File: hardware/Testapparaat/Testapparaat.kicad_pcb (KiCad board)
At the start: 2 copper layers, 127 x 142.2 mm, 115 parts, among them J1 IO_SD, J10 B-, J11 Display_shield, J12 GPIO_INPUTS, J13 FrontPanel, J14 GPIO_OUTPUT, J2 Module_1, J3 Module_2, J4 DEBUG, J5 FPC_40P_LCD_ILI9488, J6 IO_UART, J7 Emergency Stop Button, J8 CON-SOCJ-2155, J9 B+, Q1 BC817, Q2 BC817, Q3 BC817, Q4 IRFR9024N, Q5 IRFR9024N, Q6 IRFR9024N, SW1 RST, SW2 on/off switch, U1 74HC595 (SIPO Shift register), U10 LM2596S-5, U11 LM2596S-3.3, U12 74AUC1G74, U2 ESP32-WROOM-32, U4 74HC595 (SIPO Shift register), U5 TCA9534 (IO Expander), U6 74HC14, U7 TCA9534 (IO Expander), U8 74HC14, U9 74HC14

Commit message: -enh routed power section
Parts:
- C15, R19, R20: moved to B.Cu
- moved Q5 17.2 mm to (165.5, 38.3)
- moved R19 9.15 mm to (153.3, 98.2), turned to -90 degrees
- moved Q6 7.93 mm to (165.6, 45.2)
- moved Q4 6.73 mm to (165.7, 53.1)
- moved REF** 4.15 mm to (165.2, 29.5)
- moved C15 3.96 mm to (147.7, 93.3)
- moved R20 3.24 mm to (168.4, 51.7)
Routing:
- net +5VP: track 0.00 -> 39.7 mm
- net +VSW: track 0.00 -> 33.9 mm
- net +3.3VP: track 0.00 -> 20.1 mm

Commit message: -enh routed more power section
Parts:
- removed the REF** at (181.4, 124.4)
- C16, J14, R1, U4: moved to B.Cu
- moved R10 62.3 mm to (145.5, 157.2), turned to 180 degrees
- moved R9 59.0 mm to (148.0, 159.1), turned to 90 degrees
- moved C8 48.8 mm to (204.6, 133.9), turned to 90 degrees
- moved U11 38.5 mm to (163.8, 142.5), turned to 90 degrees
- moved J10 38.2 mm to (164.5, 124.4)
- moved L1 37.1 mm to (201.2, 143.3), turned to 90 degrees
- moved D1 36.1 mm to (199.9, 151.8), turned to 0 degrees
- moved C22 34.7 mm to (153.3, 36.5), turned to 90 degrees
- moved R7 31.9 mm to (151.5, 151.4)
- moved R8 30.8 mm to (150.1, 145.9)
- moved C9 27.5 mm to (179.9, 131.5), turned to 180 degrees
- moved C3 23.8 mm to (232.1, 131.7)
- moved R6 23.8 mm to (230.1, 133.0)
- moved D2 19.7 mm to (174.8, 151.5), turned to 0 degrees
- moved C2 18.3 mm to (192.6, 129.6)
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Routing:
- net +BATT: track 77.7 -> 211.1 mm
- net +5V: track 32.0 -> 160.2 mm, vias 1 -> 0
- net +VSW: track 33.9 -> 91.7 mm
- net +5VP: track 39.7 -> 96.8 mm
- net REG_EN: track 50.2 -> 0.00 mm, vias 2 -> 0
- net +3.3V: track 39.6 -> 81.7 mm, vias 1 -> 0
- net +3.3VP: track 20.1 -> 57.2 mm
- net Net-(Q3-Pad3): track 0.00 -> 22.7 mm, vias 0 -> 2
- net Net-(C2-Pad1): track 0.00 -> 22.3 mm
- net Net-(D1-Pad1): track 19.1 -> 0.00 mm
- net Net-(D4-Pad2): track 8.48 -> 0.00 mm
- net GND: track 7.77 -> 0.00 mm
- net Net-(R7-Pad2): track 7.62 -> 0.00 mm, vias 1 -> 0
- net Net-(R10-Pad1): track 6.44 -> 2.32 mm, vias 1 -> 0

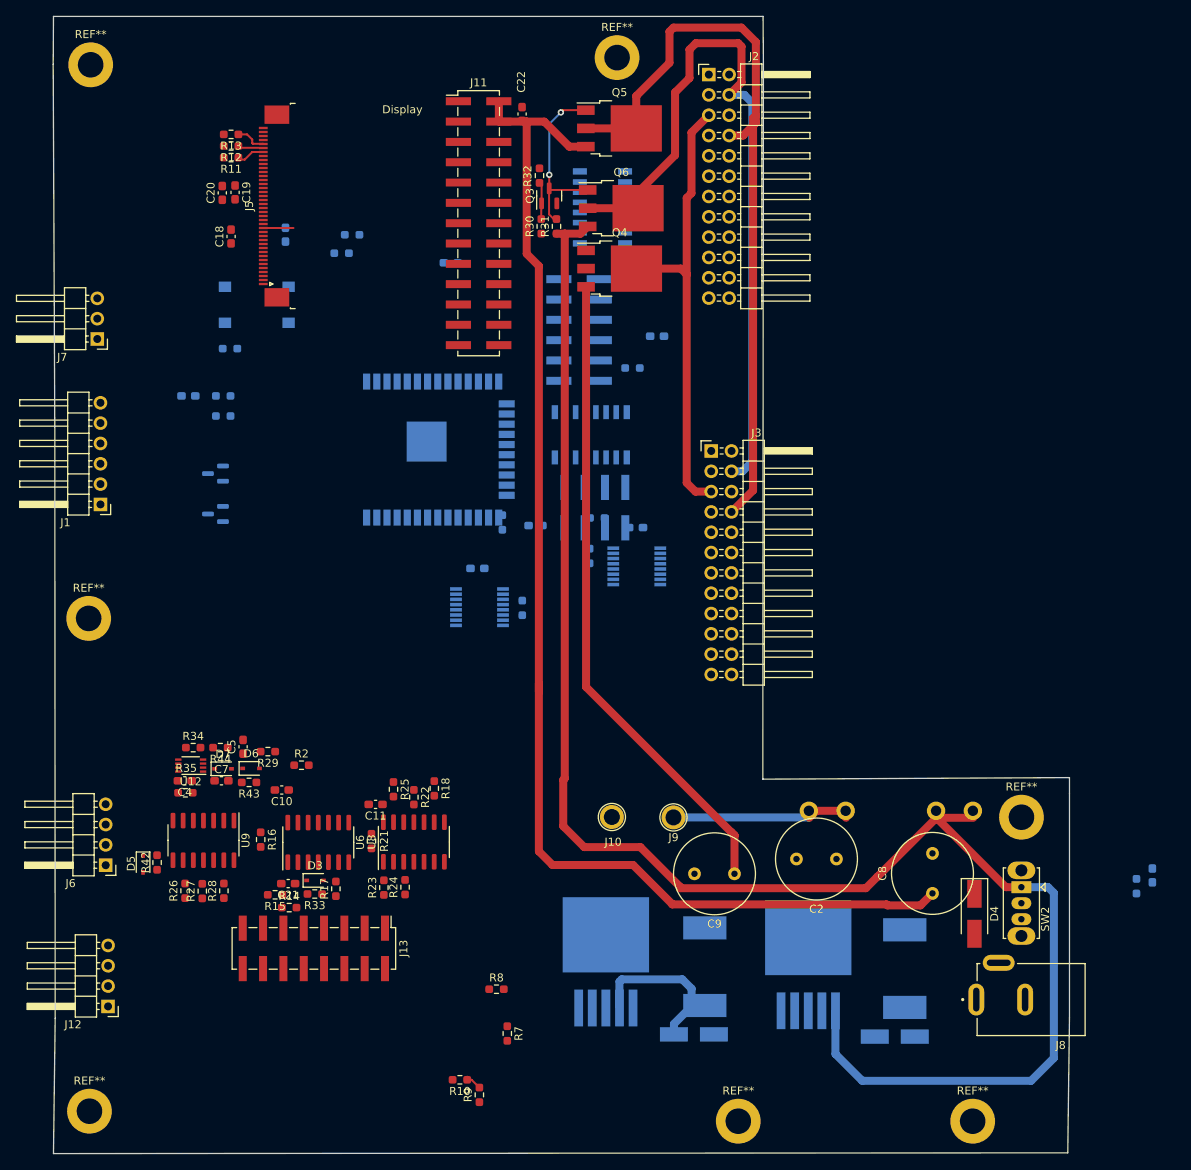
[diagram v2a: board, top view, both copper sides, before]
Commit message: -enh routed some of the module traces
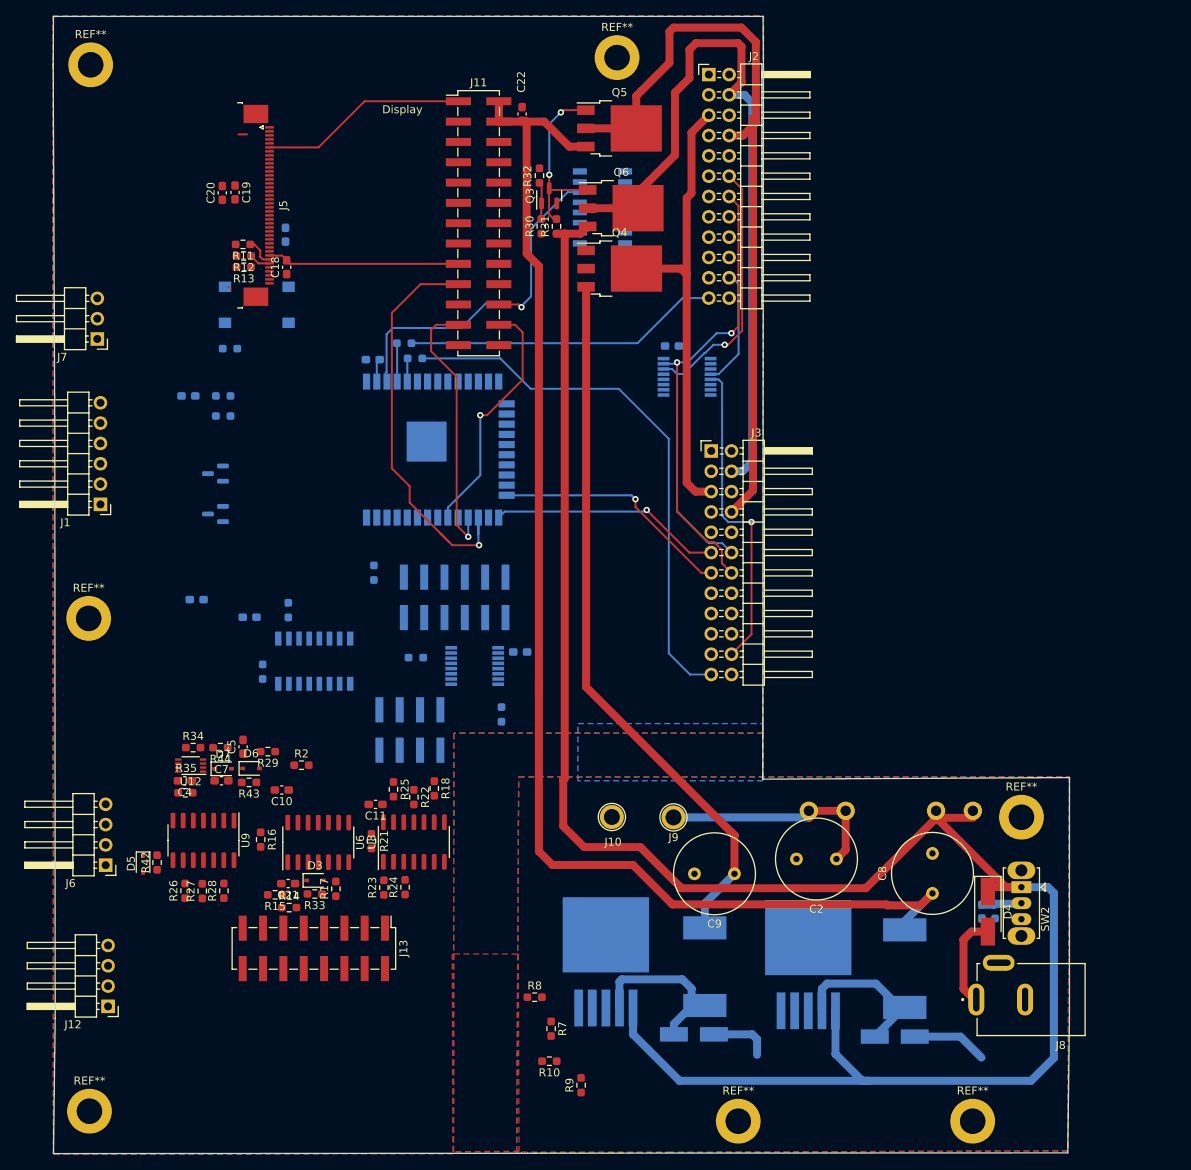
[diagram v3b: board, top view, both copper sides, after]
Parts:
- moved R1 52.6 mm to (124.1, 98.5), turned to -90 degrees
- moved U4 44.7 mm to (127.3, 104.9)
- moved U5 38.8 mm to (173.9, 69.4)
- moved C14 37.5 mm to (119.3, 99.4)
- moved J4 36.9 mm to (144.9, 96.9), turned to 90 degrees
- moved J14 36.2 mm to (139.3, 113.5)
- moved C15 35.3 mm to (112.6, 97.2)
- moved R19 33.4 mm to (120.9, 106.2)
- moved R40 28.6 mm to (140.0, 104.5)
- moved U7 23.8 mm to (147.4, 105.5)
- moved R41 22.7 mm to (150.7, 111.6)
- moved C3 21.8 mm to (210.8, 136.2)
- moved C17 21.3 mm to (153.1, 103.8)
- moved R6 17.9 mm to (212.4, 136.1)
- moved R36 17.3 mm to (139.9, 67.1)
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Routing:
- net ID_MOD_2: track 0.00 -> 68.2 mm
- net +3.3V: track 81.7 -> 142.9 mm
- net I2C_SCL: track 0.00 -> 58.4 mm, vias 0 -> 1
- net I2C_SDA: track 0.00 -> 57.6 mm, vias 0 -> 2
- net SPI_MOSI: track 0.00 -> 52.7 mm, vias 0 -> 1
- net TTL3_MOD_2: track 0.00 -> 39.8 mm, vias 0 -> 1
- net +BATT: track 211.1 -> 250.7 mm
- net ID_MOD_1: track 0.00 -> 39.5 mm
- net SPI_CLK: track 0.00 -> 33.9 mm, vias 0 -> 1
- net /Display/Display_CS: track 0.00 -> 30.9 mm, vias 0 -> 1
- net PWM2_MOD_2: track 0.00 -> 30.1 mm, vias 0 -> 1
- net PWM1_MOD_2: track 0.00 -> 29.2 mm, vias 0 -> 1
- net Net-(D1-Pad1): track 0.00 -> 19.9 mm
- net RESET: track 0.00 -> 19.1 mm
- net Display_RST: track 3.78 -> 21.3 mm, vias 0 -> 1
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- added copper zone on B.Cu, net GND
- added copper zone on F.Cu, net GND

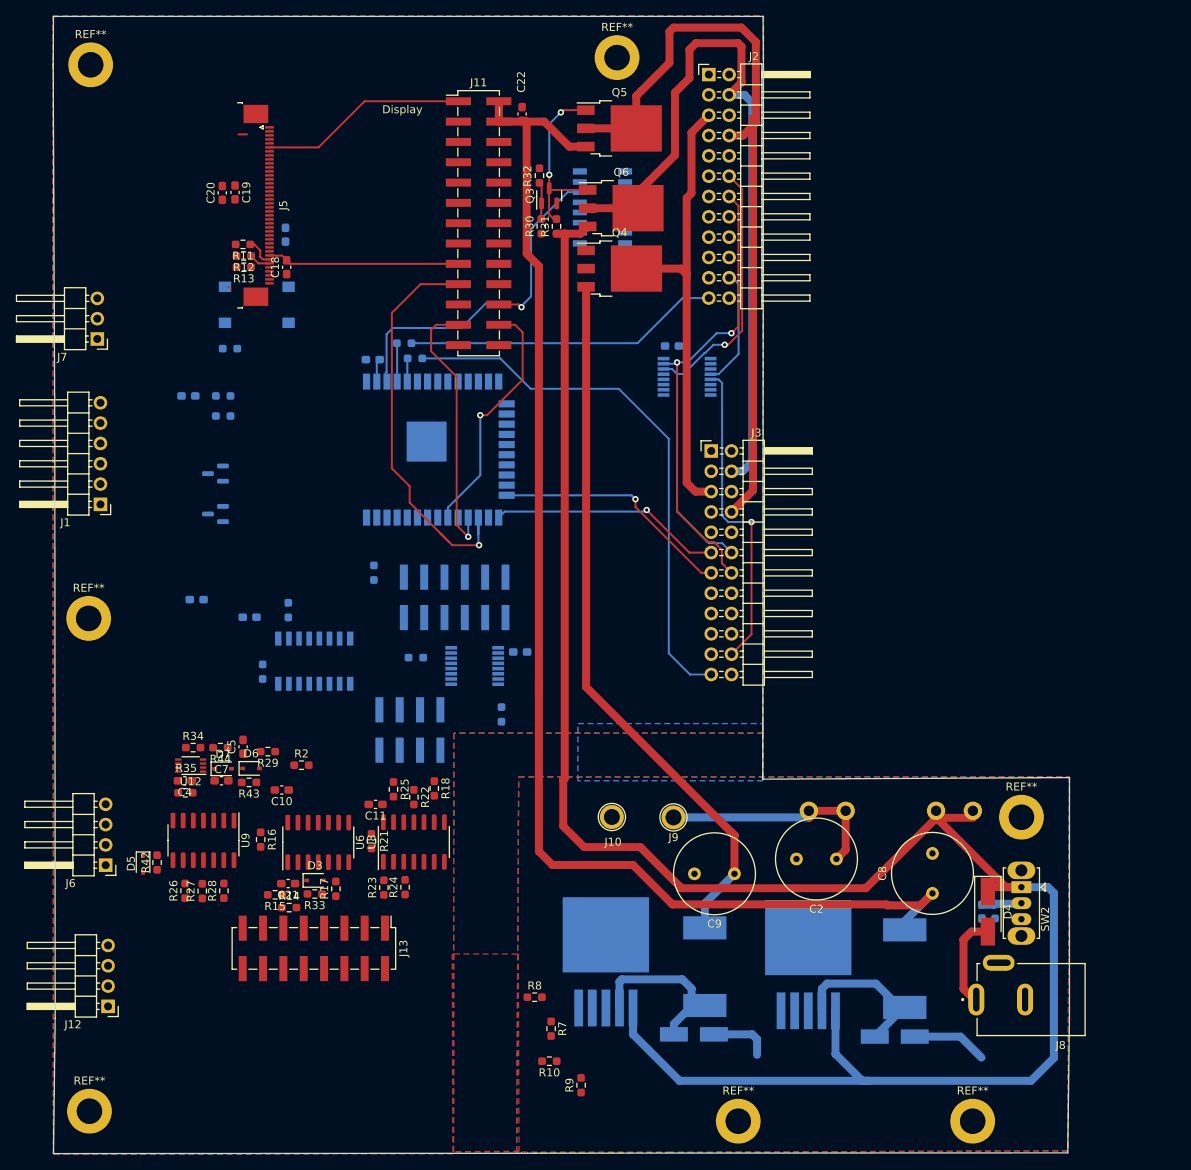
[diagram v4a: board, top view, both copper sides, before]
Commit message: -enh Routed most of the module sections
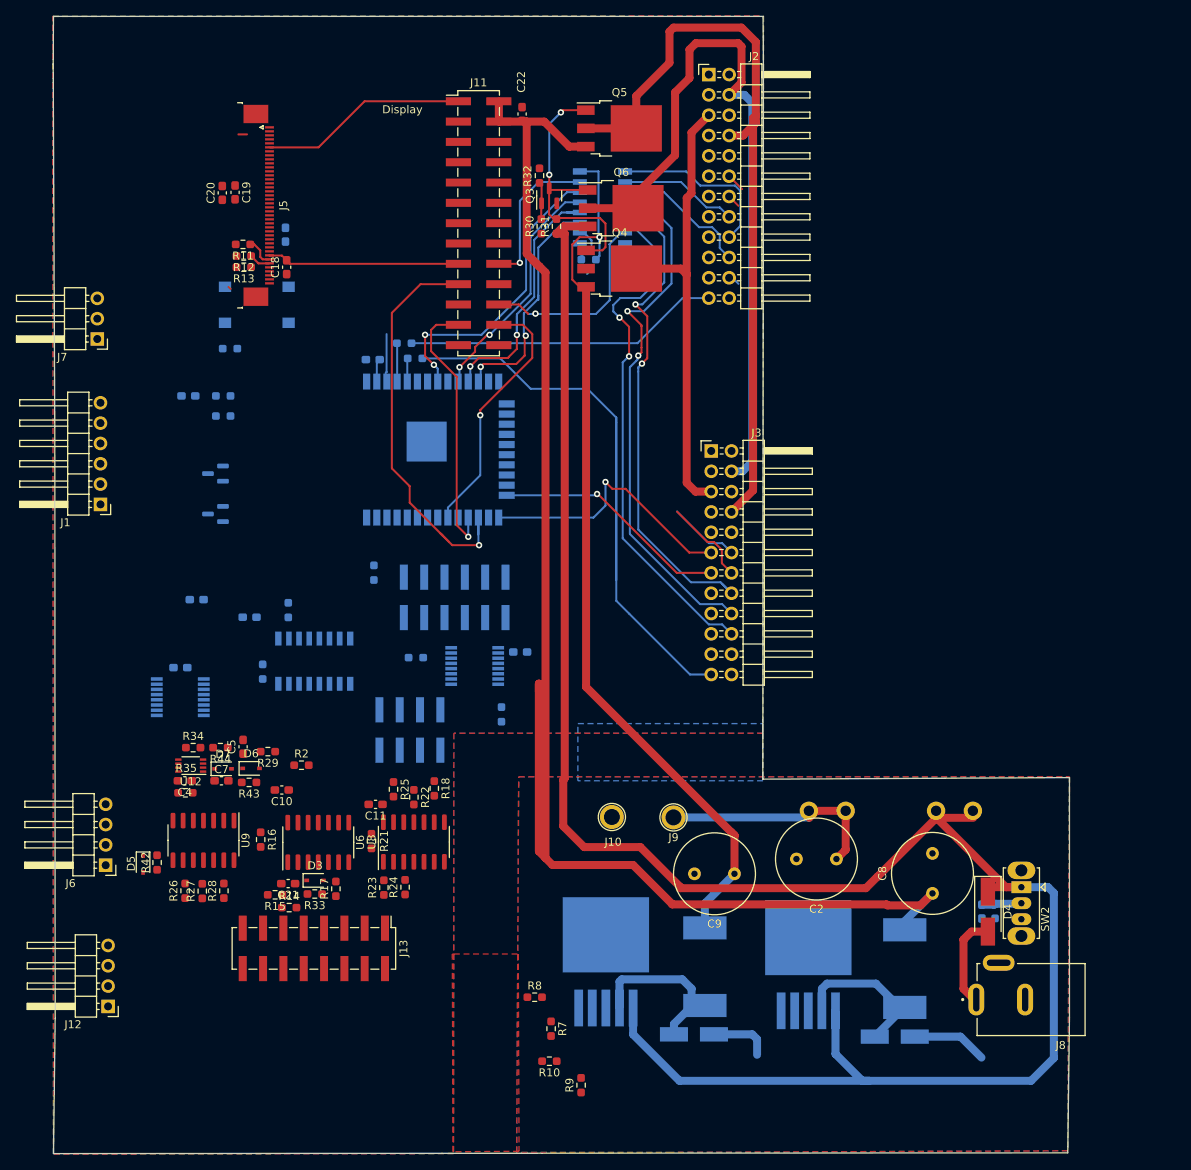
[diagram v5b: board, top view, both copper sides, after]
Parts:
- removed REF** (x7): MountingHole_3.2mm_M3_DIN965_Pad, MountingHole:MountingHole_3.2mm_M3_DIN965_Pad
- moved U5 74.9 mm to (110.6, 109.4)
- moved C16 73.4 mm to (110.6, 105.7)
- moved R20 6.54 mm to (161.6, 54.7), turned to 180 degrees
- turned U1 to -90 degrees
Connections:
- U1 pad 1: TTL2_MOD_1 -> TTL1_MOD_1
- U1 pad 15: TTL1_MOD_1 -> Display_DC
- U1 pad 2: TTL1_MOD_2 -> STATUS_MOD_1
- U1 pad 3: TTL2_MOD_2 -> TTL2_MOD_1
- U1 pad 4: STATUS_MOD_2 -> TTL1_MOD_2
- U1 pad 5: STATUS_MOD_1 -> STATUS_MOD_2
- U1 pad 6: Display_RST -> TTL2_MOD_2
- U1 pad 7: Display_DC -> Display_RST
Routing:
- net TTL1_MOD_2: track 0.00 -> 66.7 mm, vias 0 -> 2
- net TTL2_MOD_2: track 0.00 -> 65.0 mm, vias 0 -> 2
- net STATUS_MOD_2: track 0.00 -> 62.4 mm, vias 0 -> 2
- net I2C_SCL: track 58.4 -> 11.2 mm, vias 1 -> 0
- net I2C_SDA: track 57.6 -> 12.6 mm, vias 2 -> 0
- net TTL3_MOD_2: track 39.8 -> 0.00 mm, vias 1 -> 0
- net SER: track 0.00 -> 37.4 mm, vias 0 -> 2
- net RCLK: track 0.00 -> 34.4 mm, vias 0 -> 2
- net OE: track 0.00 -> 30.6 mm, vias 0 -> 2
- net SRCLK: track 0.00 -> 30.1 mm, vias 0 -> 2
- net +3.3V: track 142.9 -> 167.5 mm, vias 0 -> 1
- net +5V: track 166.2 -> 189.4 mm
- net TTL1_MOD_1: track 0.00 -> 21.8 mm
- net Display_DC: track 0.00 -> 18.9 mm, vias 0 -> 1
- net ID_MOD_2: track 68.2 -> 86.2 mm
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
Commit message: -enh Routed jtag interface and most of pwm lines modules
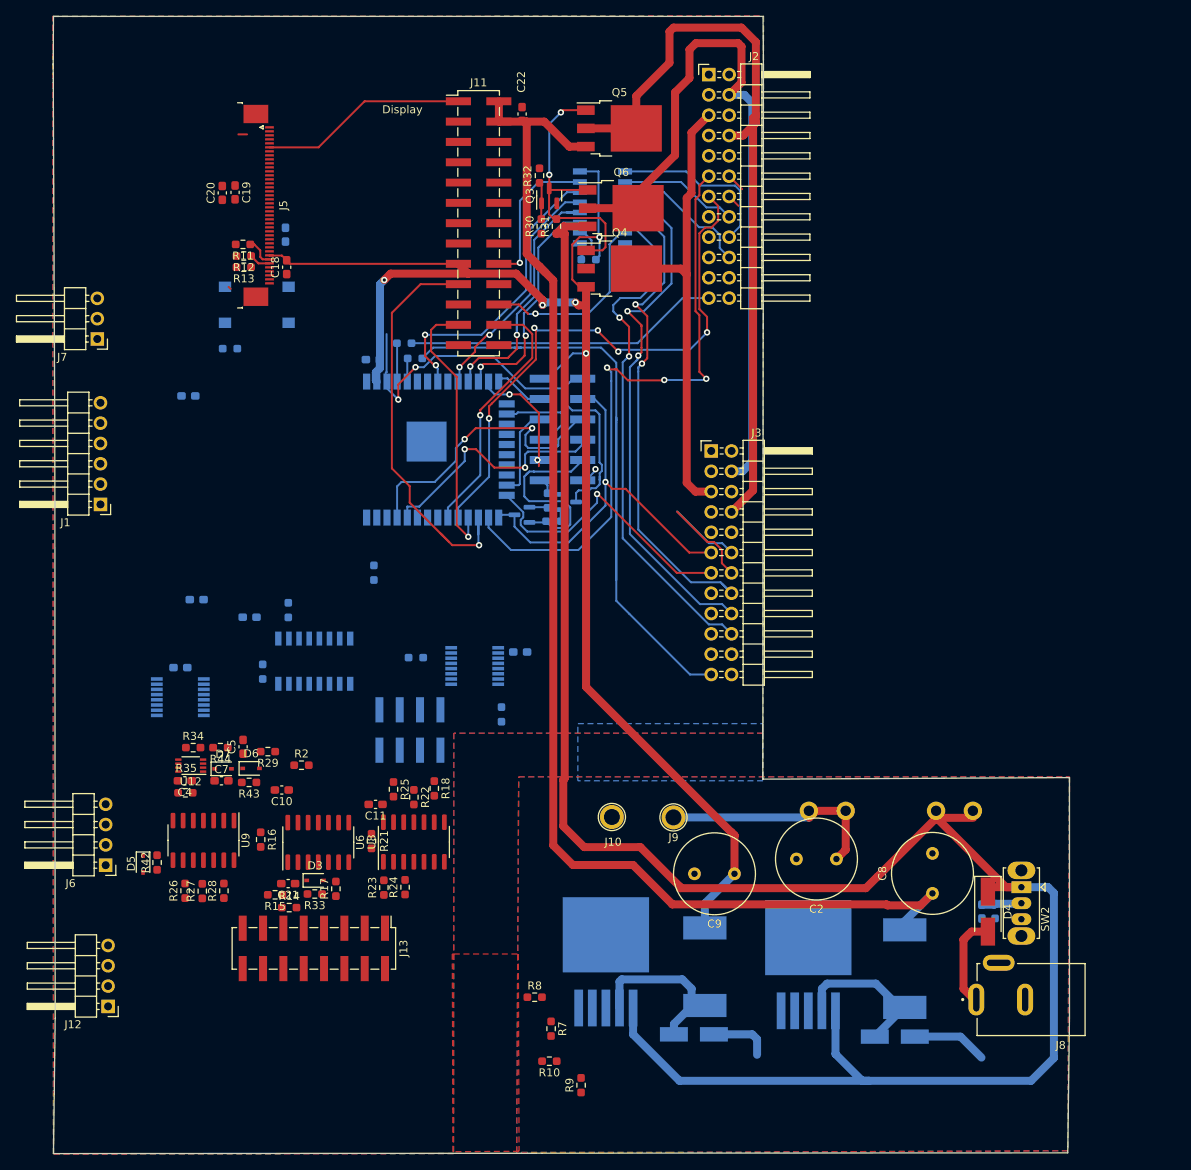
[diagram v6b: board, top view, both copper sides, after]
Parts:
- moved Q2 44.3 mm to (159.1, 85.0), turned to 0 degrees
- moved R5 44.1 mm to (157.2, 87.4), turned to 0 degrees
- moved R4 41.9 mm to (156.5, 84.8), turned to -90 degrees
- moved Q1 38.3 mm to (153.3, 86.6)
- moved J4 24.9 mm to (158.4, 75.9), turned to 180 degrees
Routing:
- net PWM1_MOD_1: track 0.00 -> 78.1 mm, vias 0 -> 3
- net PWM2_MOD_1: track 0.00 -> 71.0 mm, vias 0 -> 5
- net RESET: track 4.94 -> 57.0 mm, vias 0 -> 2
- net +3.3V: track 167.5 -> 216.6 mm, vias 1 -> 5
- net /MCU/GPIO_1/TXD0: track 0.00 -> 36.3 mm, vias 0 -> 2
- net /MCU/GPIO_3/RXD0: track 0.00 -> 31.0 mm, vias 0 -> 2
- net DTR: track 0.00 -> 25.2 mm
- net +5V: track 189.4 -> 165.9 mm
- net PWM1_MOD_2: track 33.8 -> 50.0 mm
- net /MCU/GPIO_14/JTAG_TMS: track 0.00 -> 15.4 mm, vias 0 -> 2
- net /MCU/GPIO_13/JTAG_TCK: track 0.00 -> 11.8 mm
- net /MCU/GPIO_15/JTAG_TDO: track 0.00 -> 11.5 mm
- net /MCU/GPIO_12/JTAG_TDI: track 0.00 -> 6.58 mm
- net ID_MOD_2: track 86.2 -> 92.5 mm
- net PWM2_MOD_2: track 29.5 -> 35.6 mm
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
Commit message: -enh more routing
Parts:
- C13: moved to F.Cu
- moved U5 41.8 mm to (151.7, 102.1), turned to -90 degrees
- moved R19 33.4 mm to (152.8, 96.6), turned to 180 degrees
- moved SW1 24.9 mm to (145.0, 58.5)
- moved D5 23.2 mm to (119.9, 148.7), turned to 0 degrees
- moved J14 23.1 mm to (117.2, 106.5), turned to 180 degrees
- moved R42 20.7 mm to (119.7, 147.0), turned to 180 degrees
- moved C14 14.3 mm to (133.5, 100.3), turned to -90 degrees
- moved R38 13.3 mm to (148.1, 95.0), turned to 0 degrees
- moved C13 11.9 mm to (124.6, 39.7), turned to 0 degrees
- moved R43 10.5 mm to (112.0, 112.5)
- moved R40 10.4 mm to (146.7, 96.5)
- moved R29 9.51 mm to (112.2, 114.2), turned to 0 degrees
- moved R21 8.95 mm to (141.0, 133.5), turned to 90 degrees
- moved R16 8.56 mm to (126.7, 133.2)
- moved C17 7.36 mm to (147.1, 99.5), turned to -90 degrees
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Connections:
- U5 pad 4: TTL3_MOD_1 -> EMERGENCY_STOP_BTN
- U5 pad 5: TTL3_MOD_2 -> Rotary_BTN
- U5 pad 6: EMERGENCY_STOP_BTN -> TTL3_MOD_1
- U5 pad 7: Rotary_BTN -> TTL3_MOD_2
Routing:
- net +3.3V: track 216.6 -> 348.7 mm, vias 5 -> 13
- net I2C_SDA: track 12.6 -> 143.5 mm, vias 0 -> 5
- net SPI_CLK: track 33.9 -> 150.3 mm, vias 1 -> 2
- net I2C_SCL: track 11.2 -> 126.4 mm, vias 0 -> 4
- net TTL3_MOD_1: track 0.41 -> 94.0 mm
- net SPI_MOSI: track 52.7 -> 143.6 mm, vias 1 -> 3
- net Net-(U1-Pad9): track 0.00 -> 77.4 mm, vias 0 -> 4
- net Rotary_CLK: track 0.00 -> 76.6 mm, vias 0 -> 3
- net Rotary_DT: track 0.00 -> 74.5 mm, vias 0 -> 3
- net /MCU/GPIO_1/TXD0: track 36.3 -> 100.3 mm, vias 2 -> 3
- net /MCU/GPIO_3/RXD0: track 31.0 -> 94.8 mm, vias 2 -> 3
- net SRCLK: track 30.1 -> 87.4 mm, vias 2 -> 4
- net RCLK: track 34.4 -> 90.9 mm, vias 2 -> 4
- net SPI_MISO: track 0.00 -> 51.7 mm, vias 0 -> 2
- net OE: track 30.6 -> 81.7 mm, vias 2 -> 4
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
